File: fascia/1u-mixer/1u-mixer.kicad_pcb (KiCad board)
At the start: 2 copper layers, 162.4 x 101.8 mm, 2 parts

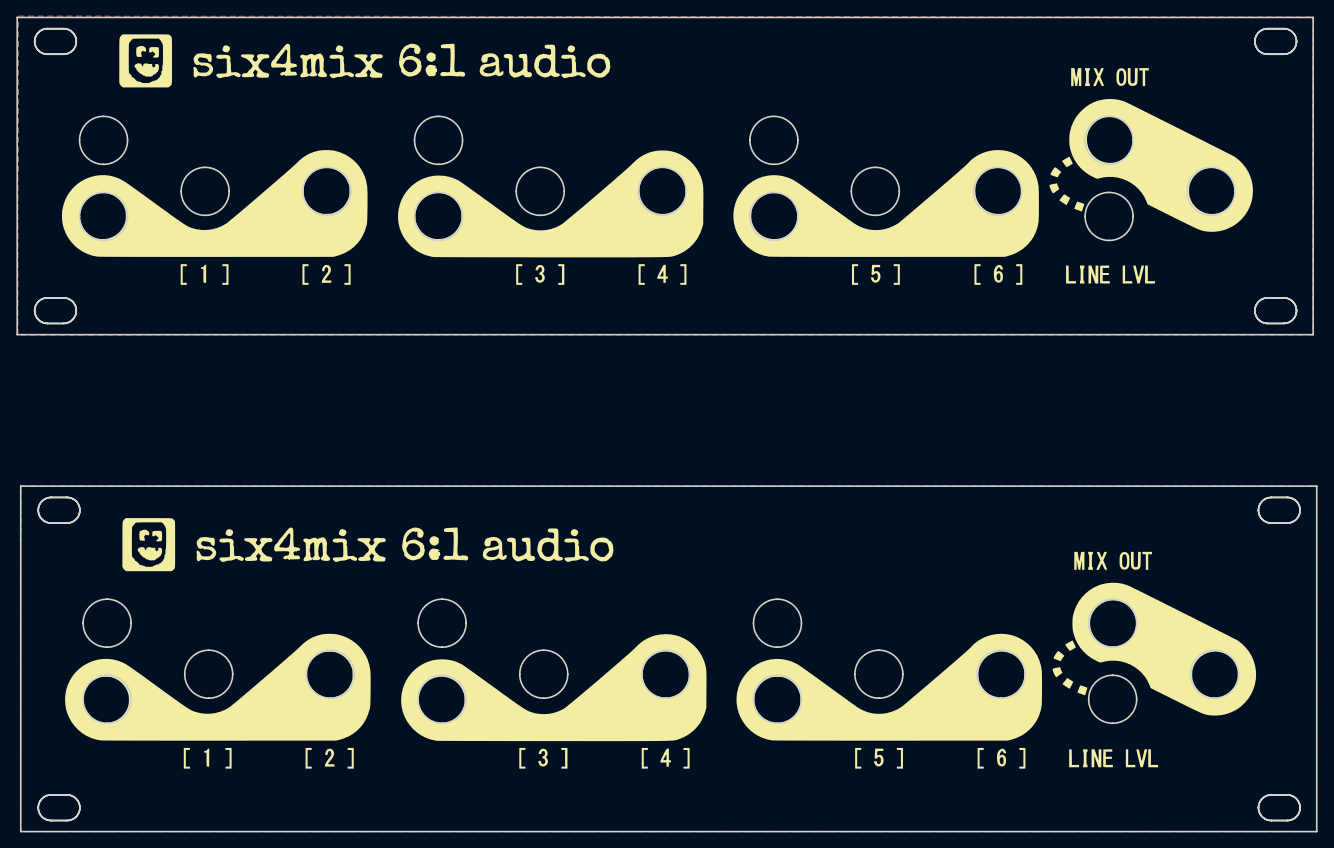
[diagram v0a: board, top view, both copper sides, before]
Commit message: 6.5mm holes
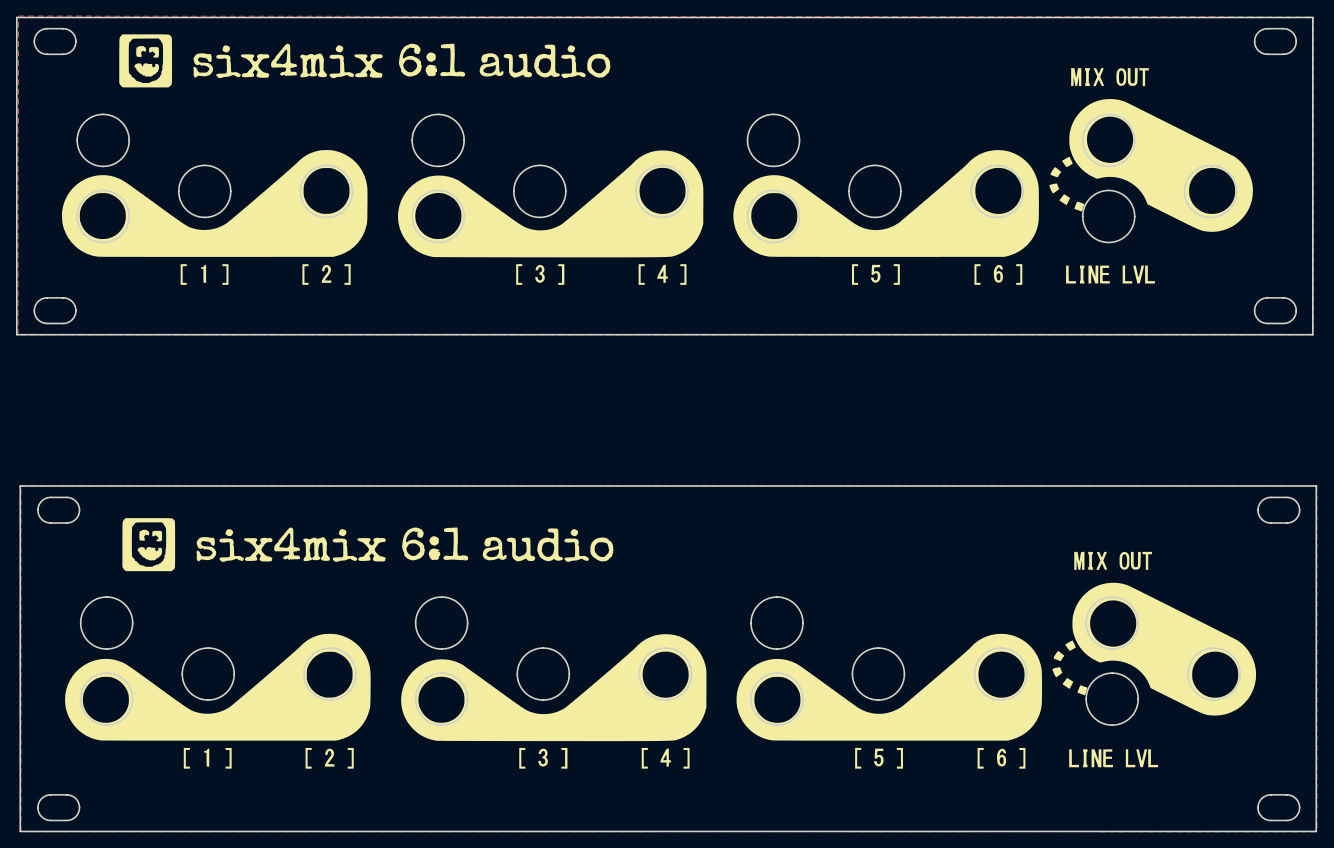
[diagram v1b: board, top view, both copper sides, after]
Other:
- board size 162.4 x 101.8 mm -> 162.4 x 101.7 mm

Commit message: Update 1u-mixer.kicad_pcb
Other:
- board size 162.4 x 101.7 mm -> 162.3 x 101.7 mm

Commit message: updates v3 larger holes
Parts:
- removed the REF** at (140.3, 41.7)
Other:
- board size 162.3 x 101.7 mm -> 162 x 43.2 mm
